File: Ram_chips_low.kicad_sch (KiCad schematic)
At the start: 10 parts, among them U25 MM5280, U26 MM5280, U27 MM5280, U28 MM5280, U40 MM5280, U41 MM5280, U42 MM5280, U43 MM5280, U6 74LS04, U7 74LS173

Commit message: Various corrections. Add new symbols and footprints
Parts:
- U25, U26, U27, U28, U40, U41, U42, U43: footprint (none) -> K-1008:DIP-22_W10.16mm_LongPads
- U6: footprint (none) -> K-1008:DIP-14_W7.62mm_LongPads
- U7: footprint (none) -> K-1008:DIP-16_W7.62mm_LongPads
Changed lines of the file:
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@@
       (effects (font (size 1.27 1.27)))
     )
-    (property "Footprint" "" (at 62.738 253.746 0)
+    (property "Footprint" "K-1008:DIP-16_W7.62mm_LongPads" (at 62.738 253.746 0)
       (effects (font (size 1.27 1.27)) hide)
     )
@@
       (effects (font (size 1.27 1.27)))
     )
-    (property "Footprint" "" (at 148.336 34.29 0)
+    (property "Footprint" "K-1008:DIP-22_W10.16mm_LongPads" (at 148.336 34.29 0)
       (effects (font (size 1.27 1.27)) hide)
     )
@@
     (pin "14")
     (pin "15")
+    (pin "16")
     (pin "17")
     (pin "19")
@@
       (effects (font (size 1.27 1.27)))
     )
-    (property "Footprint" "" (at 86.36 89.662 0)
+    (property "Footprint" "K-1008:DIP-22_W10.16mm_LongPads" (at 86.36 89.662 0)
       (effects (font (size 1.27 1.27)) hide)
     )
@@
     (pin "14")
     (pin "15")
+    (pin "16")
     (pin "17")
     (pin "19")
@@
       (effects (font (size 1.27 1.27)))
     )
-    (property "Footprint" "" (at 148.336 89.662 0)
+    (property "Footprint" "K-1008:DIP-22_W10.16mm_LongPads" (at 148.336 89.662 0)
       (effects (font (size 1.27 1.27)) hide)
     )
@@
     (pin "14")
     (pin "15")
+    (pin "16")
     (pin "17")
     (pin "19")
@@
       (effects (font (size 1.27 1.27)))
     )
-    (property "Footprint" "" (at 86.36 34.29 0)
+    (property "Footprint" "K-1008:DIP-22_W10.16mm_LongPads" (at 86.36 34.29 0)
       (effects (font (size 1.27 1.27)) hide)
     )
@@
     (pin "14")
     (pin "15")
+    (pin "16")
     (pin "17")
     (pin "19")
@@
       (effects (font (size 1.27 1.27)))
     )
-    (property "Footprint" "" (at 43.434 195.072 0)
+    (property "Footprint" "K-1008:DIP-14_W7.62mm_LongPads" (at 43.434 195.072 0)
       (effects (font (size 1.27 1.27)) hide)
     )
@@
       (effects (font (size 1.27 1.27)))
     )
-    (property "Footprint" "" (at 43.434 215.392 0)
+    (property "Footprint" "K-1008:DIP-14_W7.62mm_LongPads" (at 43.434 215.392 0)
       (effects (font (size 1.27 1.27)) hide)
     )
@@
       (effects (font (size 1.27 1.27)))
     )
-    (property "Footprint" "" (at 43.434 225.552 0)
+    (property "Footprint" "K-1008:DIP-14_W7.62mm_LongPads" (at 43.434 225.552 0)
       (effects (font (size 1.27 1.27)) hide)
     )
@@
       (effects (font (size 1.27 1.27)))
     )
-    (property "Footprint" "" (at 148.336 145.034 0)
+    (property "Footprint" "K-1008:DIP-22_W10.16mm_LongPads" (at 148.336 145.034 0)
       (effects (font (size 1.27 1.27)) hide)
     )
@@
     (pin "14")
     (pin "15")
+    (pin "16")
     (pin "17")
     (pin "19")
@@
       (effects (font (size 1.27 1.27)))
     )
-    (property "Footprint" "" (at 86.36 200.406 0)
+    (property "Footprint" "K-1008:DIP-22_W10.16mm_LongPads" (at 86.36 200.406 0)
       (effects (font (size 1.27 1.27)) hide)
     )
@@
     (pin "14")
     (pin "15")
+    (pin "16")
     (pin "17")
     (pin "19")
@@
       (effects (font (size 1.27 1.27)))
     )
-    (property "Footprint" "" (at 43.434 205.232 0)
+    (property "Footprint" "K-1008:DIP-14_W7.62mm_LongPads" (at 43.434 205.232 0)
       (effects (font (size 1.27 1.27)) hide)
     )
@@
       (effects (font (size 1.27 1.27)))
     )
-    (property "Footprint" "" (at 86.36 145.034 0)
+    (property "Footprint" "K-1008:DIP-22_W10.16mm_LongPads" (at 86.36 145.034 0)
       (effects (font (size 1.27 1.27)) hide)
     )
@@
     (pin "14")
     (pin "15")
+    (pin "16")
     (pin "17")
     (pin "19")
@@
       (effects (font (size 1.27 1.27)))
     )
-    (property "Footprint" "" (at 148.336 200.406 0)
+    (property "Footprint" "K-1008:DIP-22_W10.16mm_LongPads" (at 148.336 200.406 0)
       (effects (font (size 1.27 1.27)) hide)
     )
@@
     (pin "14")
     (pin "15")
+    (pin "16")
     (pin "17")
     (pin "19")

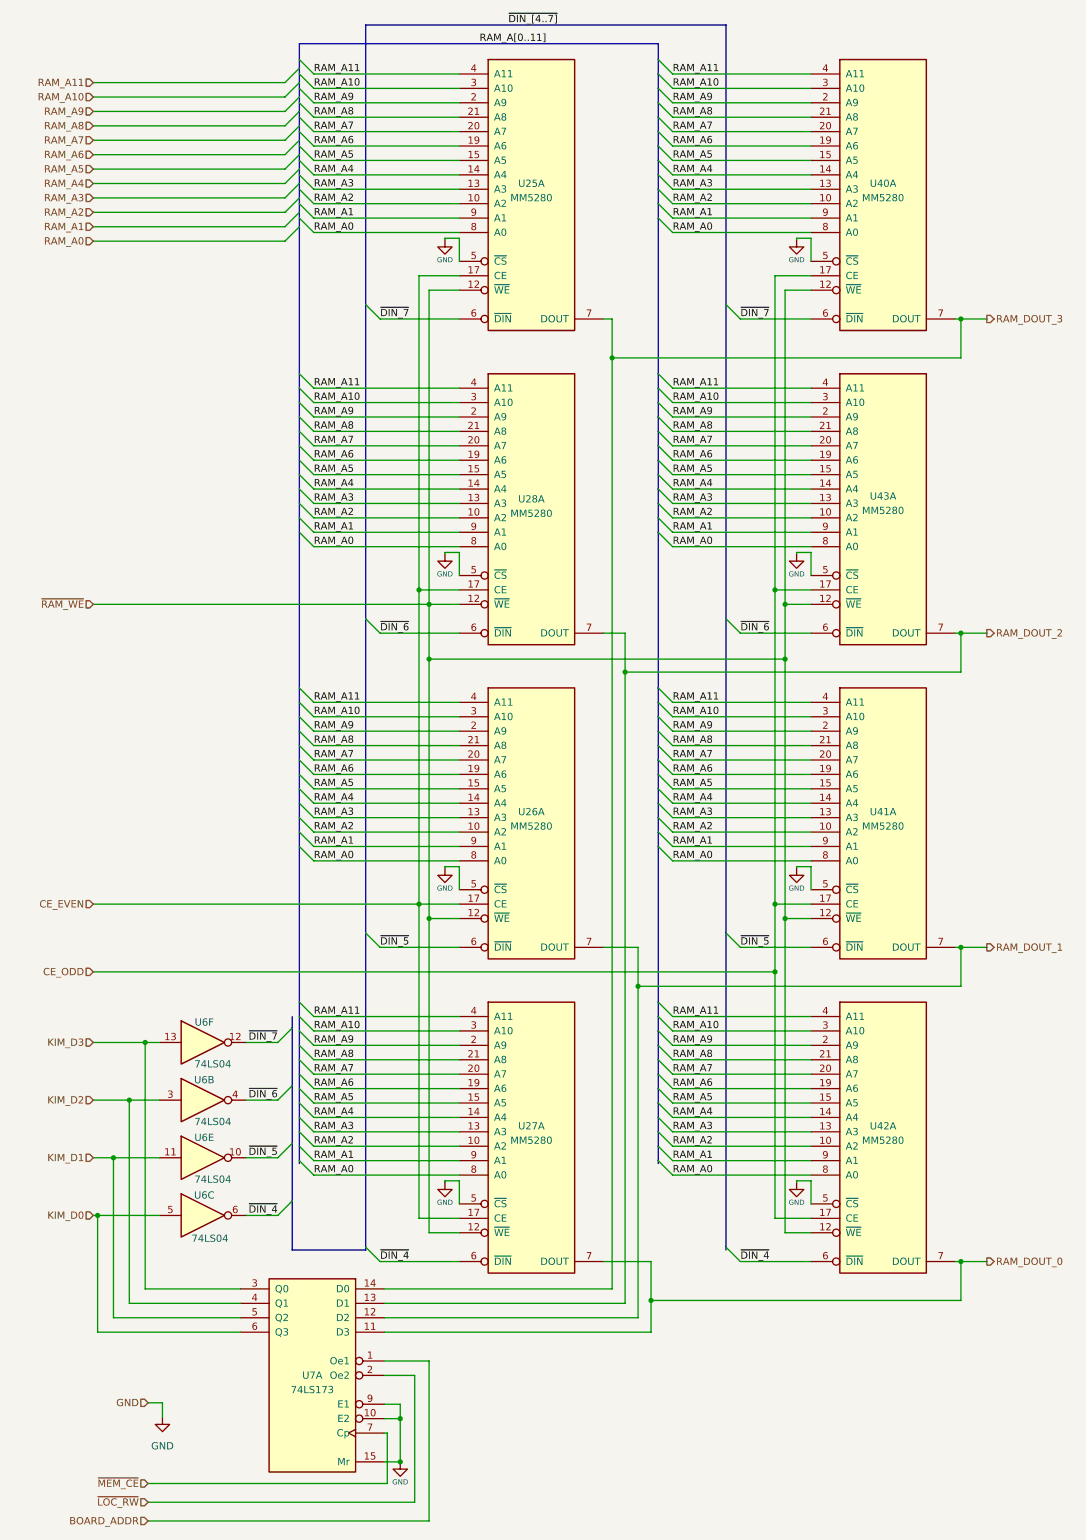
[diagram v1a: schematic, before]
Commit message: Correct address bus connections
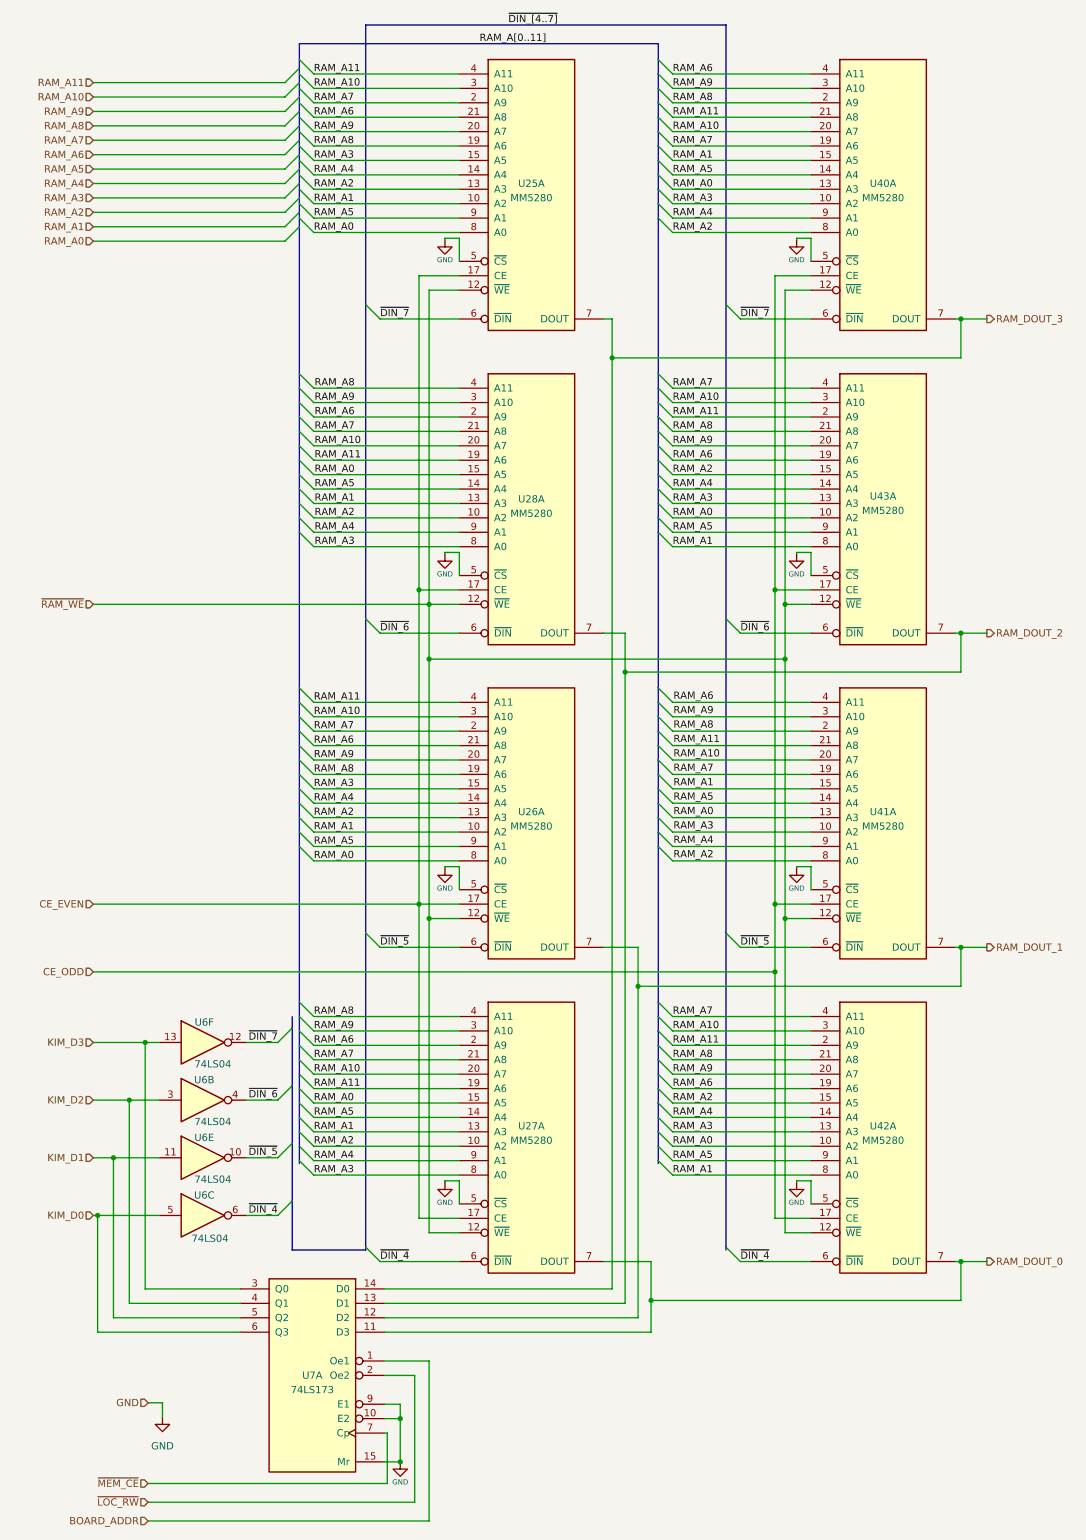
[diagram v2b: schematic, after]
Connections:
- net RAM_A0: now also U27.15 (A5), U28.15 (A5), U40.13 (A3), U42.10 (A2), U43.10 (A2); no longer U27.8 (A0), U28.8 (A0), U40.8 (A0), U41.8 (A0), U42.8 (A0), U43.8 (A0)
- net RAM_A1: now also U25.10 (A2), U26.10 (A2), U27.13 (A3), U28.13 (A3), U40.15 (A5), U42.8 (A0), U43.8 (A0); no longer U25.9 (A1), U26.9 (A1), U27.9 (A1), U28.9 (A1), U40.9 (A1), U41.9 (A1), U42.9 (A1), U43.9 (A1)
- net RAM_A10: now also U27.20 (A7), U28.20 (A7), U40.20 (A7); no longer U27.3 (A10), U28.3 (A10), U40.3 (A10), U41.3 (A10)
- net RAM_A11: now also U27.19 (A6), U28.19 (A6), U40.21 (A8), U42.2 (A9), U43.2 (A9); no longer U27.4 (A11), U28.4 (A11), U40.4 (A11), U41.4 (A11), U42.4 (A11), U43.4 (A11)
- net RAM_A2: now also U25.13 (A3), U26.13 (A3), U40.8 (A0), U42.15 (A5), U43.15 (A5); no longer U25.10 (A2), U26.10 (A2), U40.10 (A2), U41.10 (A2), U42.10 (A2), U43.10 (A2)
- net RAM_A3: now also U25.15 (A5), U26.15 (A5), U27.8 (A0), U28.8 (A0), U40.10 (A2); no longer U25.13 (A3), U26.13 (A3), U27.13 (A3), U28.13 (A3), U40.13 (A3), U41.13 (A3)
- net RAM_A4: now also U27.9 (A1), U28.9 (A1), U40.9 (A1); no longer U27.14 (A4), U28.14 (A4), U40.14 (A4), U41.14 (A4)
- net RAM_A5: now also U25.9 (A1), U26.9 (A1), U27.14 (A4), U28.14 (A4), U40.14 (A4), U42.9 (A1), U43.9 (A1); no longer U25.15 (A5), U26.15 (A5), U27.15 (A5), U28.15 (A5), U40.15 (A5), U41.15 (A5), U42.15 (A5), U43.15 (A5)
- net RAM_A6: now also U25.21 (A8), U26.21 (A8), U27.2 (A9), U28.2 (A9), U40.4 (A11); no longer U25.19 (A6), U26.19 (A6), U27.19 (A6), U28.19 (A6), U40.19 (A6), U41.19 (A6)
- net RAM_A7: now also U25.2 (A9), U26.2 (A9), U27.21 (A8), U28.21 (A8), U40.19 (A6), U42.4 (A11), U43.4 (A11); no longer U25.20 (A7), U26.20 (A7), U27.20 (A7), U28.20 (A7), U40.20 (A7), U41.20 (A7), U42.20 (A7), U43.20 (A7)
- net RAM_A8: now also U25.19 (A6), U26.19 (A6), U27.4 (A11), U28.4 (A11), U40.2 (A9); no longer U25.21 (A8), U26.21 (A8), U27.21 (A8), U28.21 (A8), U40.21 (A8), U41.21 (A8)
- net RAM_A9: now also U25.20 (A7), U26.20 (A7), U27.3 (A10), U28.3 (A10), U40.3 (A10), U42.20 (A7), U43.20 (A7); no longer U25.2 (A9), U26.2 (A9), U27.2 (A9), U28.2 (A9), U40.2 (A9), U41.2 (A9), U42.2 (A9), U43.2 (A9)

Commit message: Correct DIN_[0-3] lines
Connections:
- net ~{DIN_4} renamed ~{DIN_0}
- net ~{DIN_5} renamed ~{DIN_1}
- net ~{DIN_6} renamed ~{DIN_2}
- net ~{DIN_7} renamed ~{DIN_3}
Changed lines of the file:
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@@
     (effects (font (size 1.27 1.27)) (justify left bottom))
   )
-  (label "~{DIN_6}" (at 56.642 205.232 180) (fields_autoplaced)
+  (label "~{DIN_2}" (at 56.642 205.232 180) (fields_autoplaced)
     (effects (font (size 1.27 1.27)) (justify right bottom))
   )
@@
     (effects (font (size 1.27 1.27)) (justify left bottom))
   )
-  (label "~{DIN_5}" (at 56.642 215.392 180) (fields_autoplaced)
+  (label "~{DIN_1}" (at 56.642 215.392 180) (fields_autoplaced)
     (effects (font (size 1.27 1.27)) (justify right bottom))
   )
@@
     (effects (font (size 1.27 1.27)) (justify left bottom))
   )
-  (label "~{DIN_5}" (at 74.676 178.308 0) (fields_autoplaced)
+  (label "~{DIN_1}" (at 74.676 178.308 0) (fields_autoplaced)
     (effects (font (size 1.27 1.27)) (justify left bottom))
   )
@@
     (effects (font (size 1.27 1.27)) (justify left bottom))
   )
-  (label "~{DIN_4}" (at 74.676 233.68 0) (fields_autoplaced)
+  (label "~{DIN_0}" (at 74.676 233.68 0) (fields_autoplaced)
     (effects (font (size 1.27 1.27)) (justify left bottom))
   )
@@
     (effects (font (size 1.27 1.27)) (justify left bottom))
   )
-  (label "~{DIN_7}" (at 138.176 67.564 0) (fields_autoplaced)
+  (label "~{DIN_3}" (at 138.176 67.564 0) (fields_autoplaced)
     (effects (font (size 1.27 1.27)) (justify left bottom))
   )
@@
     (effects (font (size 1.27 1.27)) (justify left bottom))
   )
-  (label "~{DIN_5}" (at 138.176 178.308 0) (fields_autoplaced)
+  (label "~{DIN_1}" (at 138.176 178.308 0) (fields_autoplaced)
     (effects (font (size 1.27 1.27)) (justify left bottom))
   )
@@
     (effects (font (size 1.27 1.27)) (justify left bottom))
   )
-  (label "~{DIN_4}" (at 56.642 225.552 180) (fields_autoplaced)
+  (label "~{DIN_0}" (at 56.642 225.552 180) (fields_autoplaced)
     (effects (font (size 1.27 1.27)) (justify right bottom))
   )
@@
     (effects (font (size 1.27 1.27)) (justify left bottom))
   )
-  (label "~{DIN_7}" (at 56.642 195.072 180) (fields_autoplaced)
+  (label "~{DIN_3}" (at 56.642 195.072 180) (fields_autoplaced)
     (effects (font (size 1.27 1.27)) (justify right bottom))
   )
@@
     (effects (font (size 1.27 1.27)) (justify left bottom))
   )
-  (label "~{DIN_6}" (at 74.676 122.936 0) (fields_autoplaced)
+  (label "~{DIN_2}" (at 74.676 122.936 0) (fields_autoplaced)
     (effects (font (size 1.27 1.27)) (justify left bottom))
   )
@@
     (effects (font (size 1.27 1.27)) (justify left bottom))
   )
-  (label "~{DIN_7}" (at 74.676 67.564 0) (fields_autoplaced)
+  (label "~{DIN_3}" (at 74.676 67.564 0) (fields_autoplaced)
     (effects (font (size 1.27 1.27)) (justify left bottom))
   )
@@
     (effects (font (size 1.27 1.27)) (justify left bottom))
   )
-  (label "~{DIN_4}" (at 138.176 233.68 0) (fields_autoplaced)
+  (label "~{DIN_0}" (at 138.176 233.68 0) (fields_autoplaced)
     (effects (font (size 1.27 1.27)) (justify left bottom))
   )
@@
     (effects (font (size 1.27 1.27)) (justify left bottom))
   )
-  (label "~{DIN_6}" (at 138.176 122.936 0) (fields_autoplaced)
-    (effects (font (size 1.27 1.27)) (justify left bottom))
-  )
+  (label "~{DIN_2}" (at 138.176 122.936 0) (fields_autoplaced)
+    (effects (font (size 1.27 1.27)) (justify left bottom))
+  )
